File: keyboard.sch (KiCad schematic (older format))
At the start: 32 parts, among them J1 Conn_SWD, J2 Conn_ETM, J3 USB_C_Receptacle, J4 JST_PH, J5 PicoBlade, J7 2.54mm, J8 PicoBlade, J9 PicoBlade, Q1 2N7002, SW1 Slide Switch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

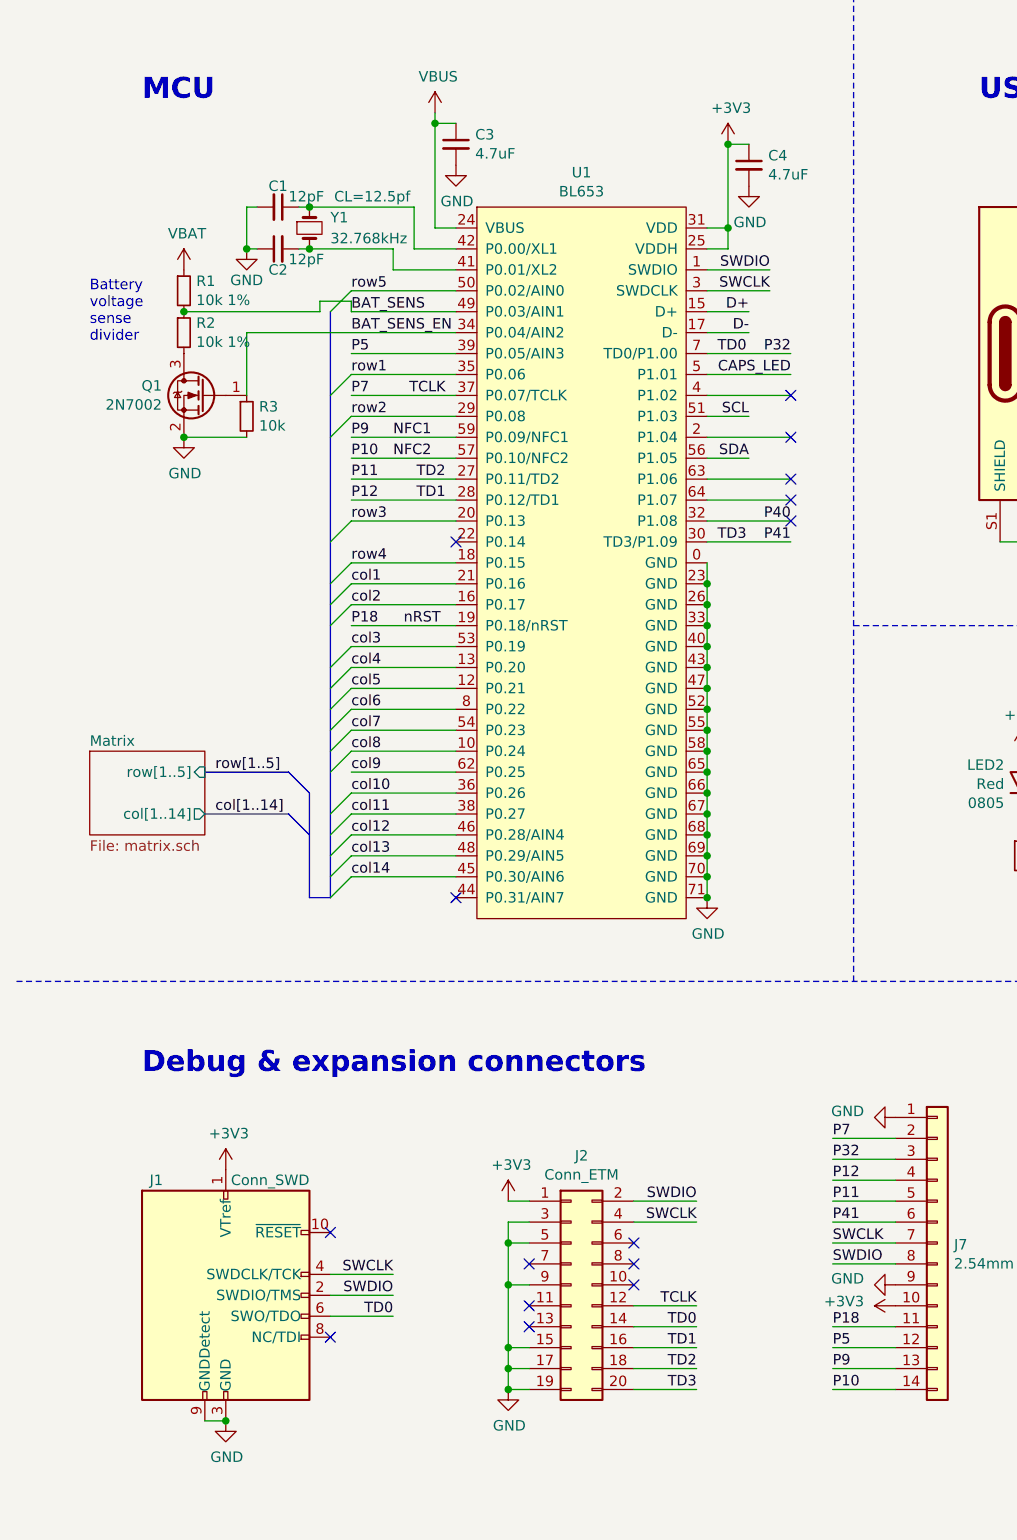
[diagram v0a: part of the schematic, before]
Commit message: Fix battery sense quiescent current draw
Q1 was useless because current still sinks through the mcu's esd diodes
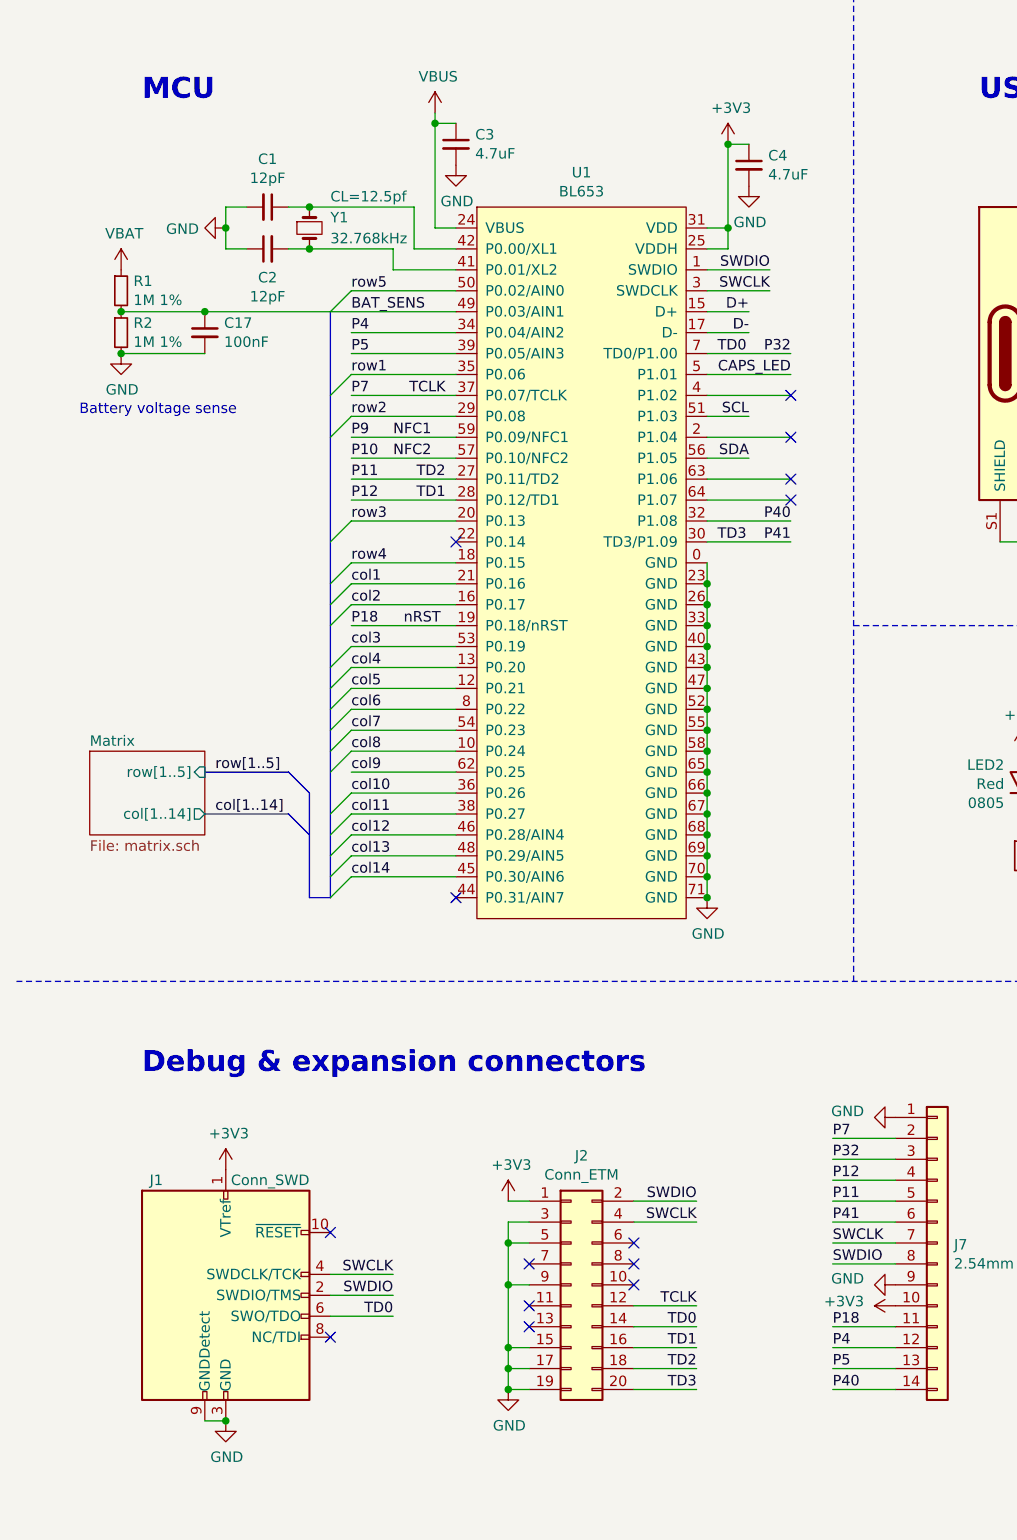
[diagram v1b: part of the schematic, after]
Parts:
- removed Q1: 2N7002, Package_TO_SOT_SMD:SOT-23, symbol Device:Q_NMOS_GSD
- removed R3: 10k, Resistor_SMD:R_0805_2012Metric, symbol Device:R_Small
- added C17: 100nF, Capacitor_SMD:C_0805_2012Metric, symbol Device:C_Small
- R1, R2: value 10k 1% -> 1M 1%
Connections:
- net BAT_SENS: now also C17.1
- net GND: now also R2.2, C17.2
- net NFC1: no longer J7.13 (Pin_13)
- net NFC2: no longer J7.14 (Pin_14)
- net P40: now also J7.14 (Pin_14)
- net P5: now also J7.13 (Pin_13); no longer J7.12 (Pin_12)
- net BAT_SENS_EN renamed P4
- net P4: now also J7.12 (Pin_12)
- no-connect marks 17 -> 16
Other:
- note added: "Battery voltage sense"
- note removed: "Battery\nvoltage\nsense\ndivider"
- moved on the sheet: C1, C2, R1, R2
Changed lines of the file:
@@
 Sheet 1 3
 Title "BLU64 Keyboard"
-Date "2021-02-14"
-Rev "A"
+Date "2021-03-07"
+Rev "B"
 Comp ""
 Comment1 "Licensed under CERN-OHL-S v2 or any later version"
@@
 L Device:C_Small C2
 U 1 1 601DEB08
-P 1650 1700
-F 0 "C2" V 1550 1700 50  0000 C CNN
-F 1 "12pF" V 1600 1650 50  0000 R CNN
-F 2 "Capacitor_SMD:C_0805_2012Metric" H 1650 1700 50  0001 C CNN
-F 3 "~" H 1650 1700 50  0001 C CNN
-	1    1650 1700
+P 1600 1700
+F 0 "C2" V 1463 1700 50  0000 C CNN
+F 1 "12pF" V 1372 1700 50  0000 C CNN
+F 2 "Capacitor_SMD:C_0805_2012Metric" H 1600 1700 50  0001 C CNN
+F 3 "~" H 1600 1700 50  0001 C CNN
+	1    1600 1700
 	0    -1   -1   0
 $EndComp
@@
 SCL
 $Comp
-L power:GND #PWR05
-U 1 1 602028FD
-P 1500 1700
-F 0 "#PWR05" H 1500 1450 50  0001 C CNN
-F 1 "GND" H 1500 1550 50  0000 C CNN
-F 2 "" H 1500 1700 50  0001 C CNN
-F 3 "" H 1500 1700 50  0001 C CNN
-	1    1500 1700
-	1    0    0    -1
-$EndComp
-$Comp
 L Device:C_Small C1
 U 1 1 601DE2F5
-P 1650 1500
-F 0 "C1" V 1550 1500 50  0000 C CNN
-F 1 "12pF" V 1600 1550 50  0000 L CNN
-F 2 "Capacitor_SMD:C_0805_2012Metric" H 1650 1500 50  0001 C CNN
-F 3 "~" H 1650 1500 50  0001 C CNN
-	1    1650 1500
+P 1600 1500
+F 0 "C1" V 1371 1500 50  0000 C CNN
+F 1 "12pF" V 1462 1500 50  0000 C CNN
+F 2 "Capacitor_SMD:C_0805_2012Metric" H 1600 1500 50  0001 C CNN
+F 3 "~" H 1600 1500 50  0001 C CNN
+	1    1600 1500
 	0    1    1    0
 $EndComp
-Connection ~ 1200 2600
-Wire Wire Line
-	1500 2600 1200 2600
-$Comp
-L Device:R_Small R3
-U 1 1 6026264E
-P 1500 2500
-F 0 "R3" H 1559 2546 50  0000 L CNN
-F 1 "10k" H 1559 2455 50  0000 L CNN
-F 2 "Resistor_SMD:R_0805_2012Metric" H 1500 2500 50  0001 C CNN
-F 3 "~" H 1500 2500 50  0001 C CNN
-	1    1500 2500
-	1    0    0    -1
-$EndComp
 Wire Wire Line
 	1800 1700 2200 1700
 Wire Wire Line
-	1500 1700 1500 1500
-Wire Wire Line
-	1500 1500 1550 1500
-Wire Wire Line
-	1550 1700 1500 1700
-Connection ~ 1500 1700
-Wire Wire Line
-	1750 1700 1800 1700
+	1700 1700 1800 1700
 Connection ~ 1800 1700
 Wire Wire Line
-	1750 1500 1800 1500
+	1700 1500 1800 1500
 Connection ~ 1800 1500
 Wire Wire Line
@@
 L Device:R_Small R1
 U 1 1 603ED6EB
-P 1200 1900
-F 0 "R1" H 1259 1946 50  0000 L CNN
-F 1 "10k 1%" H 1259 1855 50  0000 L CNN
-F 2 "Resistor_SMD:R_0805_2012Metric" H 1200 1900 50  0001 C CNN
-F 3 "~" H 1200 1900 50  0001 C CNN
-	1    1200 1900
+P 900 1900
+F 0 "R1" H 959 1946 50  0000 L CNN
+F 1 "1M 1%" H 959 1855 50  0000 L CNN
+F 2 "Resistor_SMD:R_0805_2012Metric" H 900 1900 50  0001 C CNN
+F 3 "~" H 900 1900 50  0001 C CNN
+	1    900  1900
 	1    0    0    -1
 $EndComp
@@
 L Device:R_Small R2
 U 1 1 603EDC7D
-P 1200 2100
-F 0 "R2" H 1259 2146 50  0000 L CNN
-F 1 "10k 1%" H 1259 2055 50  0000 L CNN
-F 2 "Resistor_SMD:R_0805_2012Metric" H 1200 2100 50  0001 C CNN
-F 3 "~" H 1200 2100 50  0001 C CNN
-	1    1200 2100
-	1    0    0    -1
-$EndComp
-$Comp
-L Device:Q_NMOS_GSD Q1
-U 1 1 604DF38B
-P 1300 2400
-F 0 "Q1" H 1505 2446 50  0000 L CNN
-F 1 "2N7002" H 1505 2355 50  0000 L CNN
-F 2 "Package_TO_SOT_SMD:SOT-23" H 1500 2500 50  0001 C CNN
-F 3 "~" H 1300 2400 50  0001 C CNN
-F 4 "2N7002" H 1300 2400 50  0001 C CNN "Part"
-	1    1300 2400
-	-1   0    0    -1
+P 900 2100
+F 0 "R2" H 959 2146 50  0000 L CNN
+F 1 "1M 1%" H 959 2055 50  0000 L CNN
+F 2 "Resistor_SMD:R_0805_2012Metric" H 900 2100 50  0001 C CNN
+F 3 "~" H 900 2100 50  0001 C CNN
+	1    900  2100
+	1    0    0    -1
 $EndComp
 $Comp
 L project:VBAT #PWR01
 U 1 1 6053AEAD
-P 1200 1800
-F 0 "#PWR01" H 1200 1650 50  0001 C CNN
-F 1 "VBAT" H 1215 1973 50  0000 C CNN
-F 2 "" H 1200 1800 50  0001 C CNN
-F 3 "" H 1200 1800 50  0001 C CNN
-	1    1200 1800
-	1    0    0    -1
-$EndComp
-Wire Wire Line
-	1500 2100 2500 2100
-Wire Wire Line
-	1500 2400 1500 2100
-Text Label 2000 2100 0    50   ~ 0
-BAT_SENS_EN
+P 900 1800
+F 0 "#PWR01" H 900 1650 50  0001 C CNN
+F 1 "VBAT" H 915 1973 50  0000 C CNN
+F 2 "" H 900 1800 50  0001 C CNN
+F 3 "" H 900 1800 50  0001 C CNN
+	1    900  1800
+	1    0    0    -1
+$EndComp
 Wire Bus Line
 	1300 4400 1700 4400
@@
 Entry Wire Line
 	1900 3100 2000 3000
-Connection ~ 1200 2000
-Wire Wire Line
-	1850 2000 1200 2000
-Wire Wire Line
-	1850 1950 1850 2000
-Wire Wire Line
-	2000 1950 1850 1950
-Wire Wire Line
-	2000 2000 2000 1950
-Wire Wire Line
-	2500 2000 2000 2000
+Connection ~ 900  2000
 Entry Wire Line
 	1900 2000 2000 1900
@@
 L power:GND #PWR02
 U 1 1 603F2355
-P 1200 2600
-F 0 "#PWR02" H 1200 2350 50  0001 C CNN
-F 1 "GND" H 1205 2427 50  0000 C CNN
-F 2 "" H 1200 2600 50  0001 C CNN
-F 3 "" H 1200 2600 50  0001 C CNN
-	1    1200 2600
+P 900 2200
+F 0 "#PWR02" H 900 1950 50  0001 C CNN
+F 1 "GND" H 905 2027 50  0000 C CNN
+F 2 "" H 900 2200 50  0001 C CNN
+F 3 "" H 900 2200 50  0001 C CNN
+	1    900  2200
 	1    0    0    -1
 $EndComp
@@
 $EndComp
 Text Label 4300 6950 0    50   ~ 0
+P4
+Text Label 4300 7050 0    50   ~ 0
 P5
-Text Label 4300 6850 0    50   ~ 0
-P18
-Text Label 4300 7050 0    50   ~ 0
-P9
 Text Label 4300 7150 0    50   ~ 0
-P10
+P40
 Wire Wire Line
 	4600 5950 4300 5950
@@
 	1    0    0    -1
 $EndComp
-$Comp
-L Device:C_Small C15
-U 1 1 604CAF25
-P 6000 6200
-F 0 "C15" H 5908 6200 50  0000 R CNN
-F 1 "Ctune" H 5908 6245 50  0001 R CNN
-F 2 "Capacitor_SMD:C_0805_2012Metric" H 6000 6200 50  0001 C CNN
-F 3 "~" H 6000 6200 50  0001 C CNN
-F 4 "DNP" H 6000 6200 50  0001 C CNN "Variant"
-	1    6000 6200
-	-1   0    0    1
-$EndComp
-$Comp
-L Device:C_Small C14
-U 1 1 604CD1C7
-P 6000 5900
-F 0 "C14" H 5908 5900 50  0000 R CNN
-F 1 "Ctune" H 5908 5945 50  0001 R CNN
-F 2 "Capacitor_SMD:C_0805_2012Metric" H 6000 5900 50  0001 C CNN
-F 3 "~" H 6000 5900 50  0001 C CNN
-F 4 "DNP" H 6000 5900 50  0001 C CNN "Variant"
-	1    6000 5900
-	-1   0    0    1
-$EndComp
 Wire Wire Line
 	5700 6100 6000 6100
@@
 	1    0    0    -1
 $EndComp
-NoConn ~ 4100 3000
 NoConn ~ 4100 2900
 NoConn ~ 4100 2800
@@
 Wire Notes Line
 	4400 3500 6950 3500
-Text Notes 750  2150 0    50   ~ 0
-Battery\nvoltage\nsense\ndivider
+Text Notes 700  2500 0    50   ~ 0
+Battery voltage sense
 Text Label 4100 3000 2    50   ~ 0
 P40
@@
 F3 "col[1..14]" O R 1300 4400 50
 $EndSheet
-Wire Bus Line
-	1800 4300 1800 4800
-Wire Bus Line
-	1900 2000 1900 4800
+Wire Wire Line
+	2000 2100 2500 2100
+Text Label 2000 2100 0    50   ~ 0
+P4
+$Comp
+L Device:C_Small C17
+U 1 1 60484F5F
+P 1300 2100
+F 0 "C17" H 1392 2146 50  0000 L CNN
+F 1 "100nF" H 1392 2055 50  0000 L CNN
+F 2 "Capacitor_SMD:C_0805_2012Metric" H 1300 2100 50  0001 C CNN
+F 3 "~" H 1300 2100 50  0001 C CNN
+	1    1300 2100
+	1    0    0    -1
+$EndComp
+Connection ~ 1300 2000
+Wire Wire Line
+	1300 2000 900  2000
+Wire Wire Line
+	1300 2200 900  2200
+Connection ~ 900  2200
+Wire Wire Line
+	1400 1600 1400 1500
+Connection ~ 1400 1600
+Wire Wire Line
+	1500 1700 1400 1700
+Wire Wire Line
+	1400 1500 1500 1500
+Wire Wire Line
+	1400 1700 1400 1600
+$Comp
+L power:GND #PWR05
+U 1 1 602028FD
+P 1400 1600
+F 0 "#PWR05" H 1400 1350 50  0001 C CNN
+F 1 "GND" V 1405 1472 50  0000 R CNN
+F 2 "" H 1400 1600 50  0001 C CNN
+F 3 "" H 1400 1600 50  0001 C CNN
+	1    1400 1600
+	0    1    1    0
+$EndComp
 $Comp
 L Device:Crystal_Small Y1
@@
 F 2 "Crystal:Crystal_SMD_3215-2Pin_3.2x1.5mm" H 1800 1600 50  0001 C CNN
 F 3 "~" H 1800 1600 50  0001 C CNN
-F 4 "CL=12.5pf" V 1650 1900 50  0000 C CNN "Comment"
+F 4 "CL=12.5pf" V 1650 1700 50  0000 L CNN "Comment"
 	1    1800 1600
 	0    1    1    0
 $EndComp
+Wire Wire Line
+	1300 2000 2500 2000
+Wire Bus Line
+	1800 4300 1800 4800
+Wire Bus Line
+	1900 2000 1900 4800
+Text Label 4300 6850 0    50   ~ 0
+P18
+$Comp
+L Device:C_Small C14
+U 1 1 604CD1C7
+P 6000 5900
+F 0 "C14" H 5908 5900 50  0000 R CNN
+F 1 "Ctune" H 5908 5945 50  0001 R CNN
+F 2 "Capacitor_SMD:C_0805_2012Metric" H 6000 5900 50  0001 C CNN
+F 3 "~" H 6000 5900 50  0001 C CNN
+F 4 "DNP" H 6000 5900 50  0001 C CNN "Variant"
+	1    6000 5900
+	-1   0    0    1
+$EndComp
+$Comp
+L Device:C_Small C15
+U 1 1 604CAF25
+P 6000 6200
+F 0 "C15" H 5908 6200 50  0000 R CNN
+F 1 "Ctune" H 5908 6245 50  0001 R CNN
+F 2 "Capacitor_SMD:C_0805_2012Metric" H 6000 6200 50  0001 C CNN
+F 3 "~" H 6000 6200 50  0001 C CNN
+F 4 "DNP" H 6000 6200 50  0001 C CNN "Variant"
+	1    6000 6200
+	-1   0    0    1
+$EndComp
 $EndSCHEMATC

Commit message: archive footprints and schematics symbols
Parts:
- C1, C14, C15, C16, C17, C2, C3, C4: footprint Capacitor_SMD:C_0805_2012Metric -> archive:C_0805_2012Metric; symbol Device:C_Small -> archive:Device_C_Small
- D35, D36: footprint Diode_SMD:D_SOD-123 -> archive:D_SOD-123; symbol Device:D_Small -> archive:Device_D_Small
- F1: footprint Fuse:Fuseholder_Littelfuse_Nano2_154x -> archive:Fuseholder_Littelfuse_Nano2_154x; symbol Device:Fuse -> archive:Device_Fuse
- J1: footprint Connector_PinHeader_1.27mm:PinHeader_2x05_P1.27mm_Vertical_SMD -> archive:PinHeader_2x05_P1.27mm_Vertical_SMD; symbol Connector:Conn_ARM_JTAG_SWD_10 -> archive:Connector_Conn_ARM_JTAG_SWD_10
- J2: footprint Connector_PinHeader_1.27mm:PinHeader_2x10_P1.27mm_Vertical_SMD -> archive:PinHeader_2x10_P1.27mm_Vertical_SMD; symbol Connector_Generic:Conn_02x10_Odd_Even -> archive:Connector_Generic_Conn_02x10_Odd_Even
- J3: footprint Connector_USB:USB_C_Receptacle_HRO_TYPE-C-31-M-12 -> archive:USB_C_Receptacle_HRO_TYPE-C-31-M-12; symbol Connector:USB_C_Receptacle_USB2.0 -> archive:Connector_USB_C_Receptacle_USB2.0
- J4: footprint Connector_JST:JST_PH_S2B-PH-SM4-TB_1x02-1MP_P2.00mm_Horizontal -> archive:JST_PH_S2B-PH-SM4-TB_1x02-1MP_P2.00mm_Horizontal; symbol Connector_Generic:Conn_01x02 -> archive:Connector_Generic_Conn_01x02
- J5, J8, J9: footprint Connector_Molex:Molex_PicoBlade_53261-0271_1x02-1MP_P1.25mm_Horizontal -> archive:Molex_PicoBlade_53261-0271_1x02-1MP_P1.25mm_Horizontal; symbol Connector_Generic:Conn_01x02 -> archive:Connector_Generic_Conn_01x02
- J7: footprint Connector_PinHeader_2.54mm:PinHeader_1x14_P2.54mm_Vertical -> archive:PinHeader_1x14_P2.54mm_Vertical; symbol Connector_Generic:Conn_01x14 -> archive:Connector_Generic_Conn_01x14
- LED2: footprint LED_SMD:LED_0805_2012Metric -> archive:LED_0805_2012Metric; symbol Device:LED -> archive:Device_LED
- LED3: footprint LED_THT:LED_D3.0mm -> archive:LED_D3.0mm; symbol Device:LED -> archive:Device_LED
- R1, R14, R15, R16, R2, R4, R5: footprint Resistor_SMD:R_0805_2012Metric -> archive:R_0805_2012Metric; symbol Device:R_Small -> archive:Device_R_Small
- SW1: footprint project:SW_OS102011MS2QN1 -> archive:SW_OS102011MS2QN1; symbol Switch:SW_SPDT -> archive:Switch_SW_SPDT
- U1: footprint project:Laird_BL653 -> archive:Laird_BL653; symbol project:BL653 -> archive:project_BL653
- Y1: footprint Crystal:Crystal_SMD_3215-2Pin_3.2x1.5mm -> archive:Crystal_SMD_3215-2Pin_3.2x1.5mm; symbol Device:Crystal_Small -> archive:Device_Crystal_Small

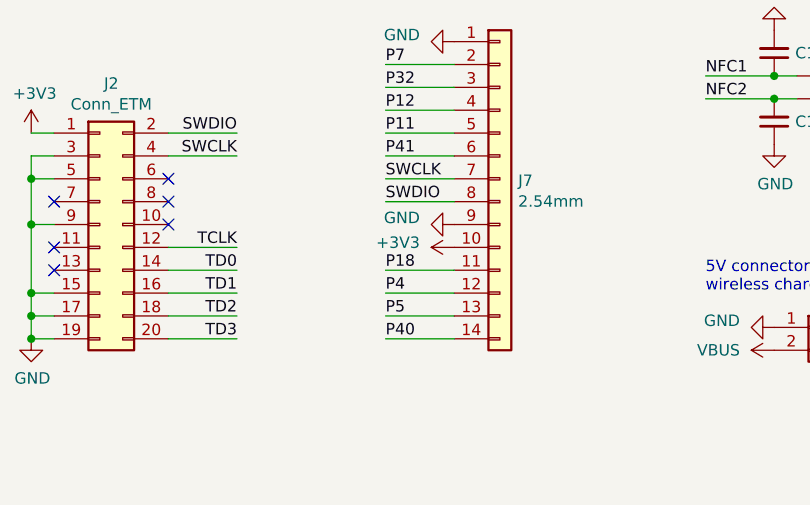
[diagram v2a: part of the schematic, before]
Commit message: small change to expansion header pinout
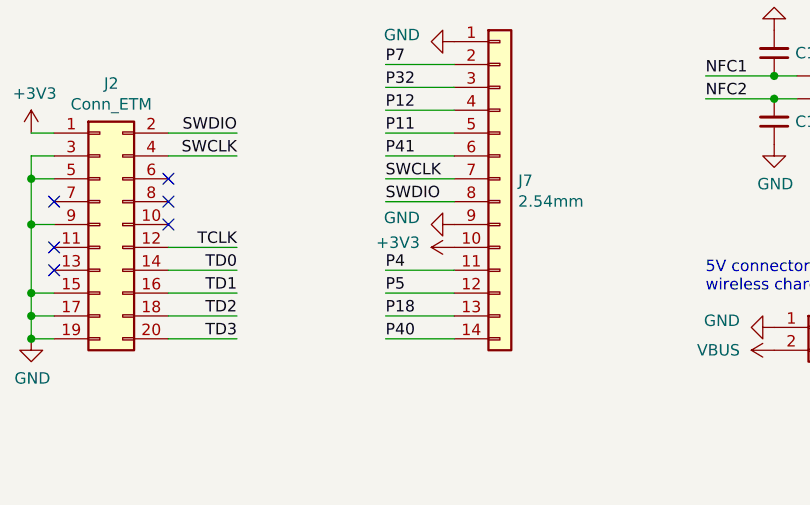
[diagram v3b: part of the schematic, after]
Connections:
- net P18: now also J7.13 (Pin_13); no longer J7.11 (Pin_11)
- net P4: now also J7.11 (Pin_11); no longer J7.12 (Pin_12)
- net P5: now also J7.12 (Pin_12); no longer J7.13 (Pin_13)
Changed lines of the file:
@@
 	0    1    1    0
 $EndComp
+Text Label 4300 6850 0    50   ~ 0
+P4
 Text Label 4300 6950 0    50   ~ 0
-P4
-Text Label 4300 7050 0    50   ~ 0
 P5
 Text Label 4300 7150 0    50   ~ 0
@@
 	4600 6550 4300 6550
 Wire Wire Line
+	4600 7050 4300 7050
+Wire Wire Line
 	4600 6850 4300 6850
 Wire Wire Line
 	4600 6950 4300 6950
-Wire Wire Line
-	4600 7050 4300 7050
 Wire Wire Line
 	4600 7150 4300 7150
@@
 	0    1    1    0
 $EndComp
-Wire Wire Line
-	1300 2000 2500 2000
-Wire Bus Line
-	1800 4300 1800 4800
-Wire Bus Line
-	1900 2000 1900 4800
-Text Label 4300 6850 0    50   ~ 0
+Text Label 4300 7050 0    50   ~ 0
 P18
 $Comp
@@
 	-1   0    0    1
 $EndComp
+Wire Wire Line
+	1300 2000 2500 2000
+Wire Bus Line
+	1800 4300 1800 4800
+Wire Bus Line
+	1900 2000 1900 4800
 $EndSCHEMATC
